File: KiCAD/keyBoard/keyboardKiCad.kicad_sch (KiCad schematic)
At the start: 183 parts, among them SW1 RotaryEncoder_Switch_MP

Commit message: Keyboard routing initially complete
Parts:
- D1, D10, D11, D12, D13, D14, D15, D16, D17, D18, D19, D2, D20, D21, D22, D23, D24, D25, D26, D27, D28, D29, D3, D30, D31, D32, D33, D34, D35, D36, D37, D38, D39, D4, D40, D41, D42, D43, D44, D45, D46, D47, D48, D49, D5, D50, D51, D52, D53, D54, D55, D56, D57, D58, D59, D6, D60, D61, D62, D63, D64, D66, D67, D68, D69, D7, D70, D71, D72, D73, D74, D75, D76, D77, D78, D79, D8, D80, D81, D82, D83, D84, D9: footprint Diode_THT:D_DO-35_SOD27_P10.16mm_Horizontal -> kbProjectLib/lcscImports:DO-35_BD2.0-L4.0-P8.00-D0.5-FD
- S1, S3, S72: footprint PCM_Switch_Keyboard_Kailh:SW_Kailh_Choc_V2_1.50u -> kbProjectLib/keyswitches:SW_Kailh_Choc_V2_1.50u
- S10, S12, S13, S14, S15, S16, S18, S19, S2, S20, S21, S22, S23, S24, S25, S26, S27, S28, S29, S30, S31, S32, S34, S35, S36, S37, S38, S39, S40, S41, S42, S43, S44, S45, S46, S47, S48, S49, S50, S51, S52, S53, S54, S55, S56, S57, S59, S60, S61, S62, S64, S65, S66, S67, S7, S70, S73, S74, S75, S76, S77, S78, S79, S8, S80, S81, S82, S83, S9: footprint PCM_Switch_Keyboard_Kailh:SW_Kailh_Choc_V2_1.00u -> kbProjectLib/keyswitches:SW_Kailh_Choc_V2_1.00u
- S11, S17, S58: footprint PCM_Switch_Keyboard_Kailh:SW_Kailh_Choc_V2_1.25u -> kbProjectLib/keyswitches:SW_Kailh_Choc_V2_1.25u
- S33: footprint PCM_Switch_Keyboard_Kailh:SW_Kailh_Choc_V2_6.25u -> kbProjectLib/keyswitches:SW_Kailh_Choc_V2_6.25u
- S4: footprint PCM_Switch_Keyboard_Kailh:SW_Kailh_Choc_V2_1.75u -> kbProjectLib/keyswitches:SW_Kailh_Choc_V2_1.75u
- S5, S68: footprint PCM_Switch_Keyboard_Kailh:SW_Kailh_Choc_V2_2.25u -> kbProjectLib/keyswitches:SW_Kailh_Choc_V2_2.25u
- S6, S69, S71: footprint PCM_Switch_Keyboard_Kailh:SW_Kailh_Choc_V2_2.00u -> kbProjectLib/keyswitches:SW_Kailh_Choc_V2_2.00u
- S63: footprint PCM_Switch_Keyboard_Kailh:SW_Kailh_Choc_V2_2.75u -> kbProjectLib/keyswitches:SW_Kailh_Choc_V2_2.75u
- SW1: footprint Rotary_Encoder:RotaryEncoder_Alps_EC11E-Switch_Vertical_H20mm -> kbProjectLib/lcscImports:SW-TH_EC11XXXXXXXX
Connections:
- net ROW1: no longer S54.1, S7.1
- net ROW2: now also S54.1, S7.1; no longer S55.1, S8.1
- net ROW3: now also S55.1, S8.1; no longer S56.1, S9.1
- net ROW4: now also S56.1, S9.1; no longer S10.1, S57.1
- net ROW5: now also S10.1, S57.1; no longer S11.1, S58.1
- net ROW6: now also S11.1, S58.1

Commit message: saving before running 3d file fixing script
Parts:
- removed H10, H11, H12, H9: (no value), ScottoKeebs_Stabilizer:Stabilizer_MX_2.00u, symbol ScottoKeebs:Placeholder_Mounting_Hole
- removed H13, H14: (no value), ScottoKeebs_Cutout:Cutout_Stabilizer_3.00u, symbol ScottoKeebs:Placeholder_Mounting_Hole
- removed H15, H16: (no value), ScottoKeebs_Stabilizer:Stabilizer_MX_6.25u, symbol ScottoKeebs:Placeholder_Mounting_Hole
- H1, H2, H3, H4, H5, H6: footprint ScottoKeebs_Stabilizer:Stabilizer_MX_2.00u -> kbProjectLib/keyswitches:Stabilizer_Cherry_MX_2.00u
- H7: footprint ScottoKeebs_Stabilizer:Stabilizer_MX_2.00u -> kbProjectLib/keyswitches:Stabilizer_Cherry_MX_3.00u
- H8: footprint ScottoKeebs_Stabilizer:Stabilizer_MX_2.00u -> kbProjectLib/keyswitches:Stabilizer_Cherry_MX_6.25u
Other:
- moved on the sheet: H6, H7, H8

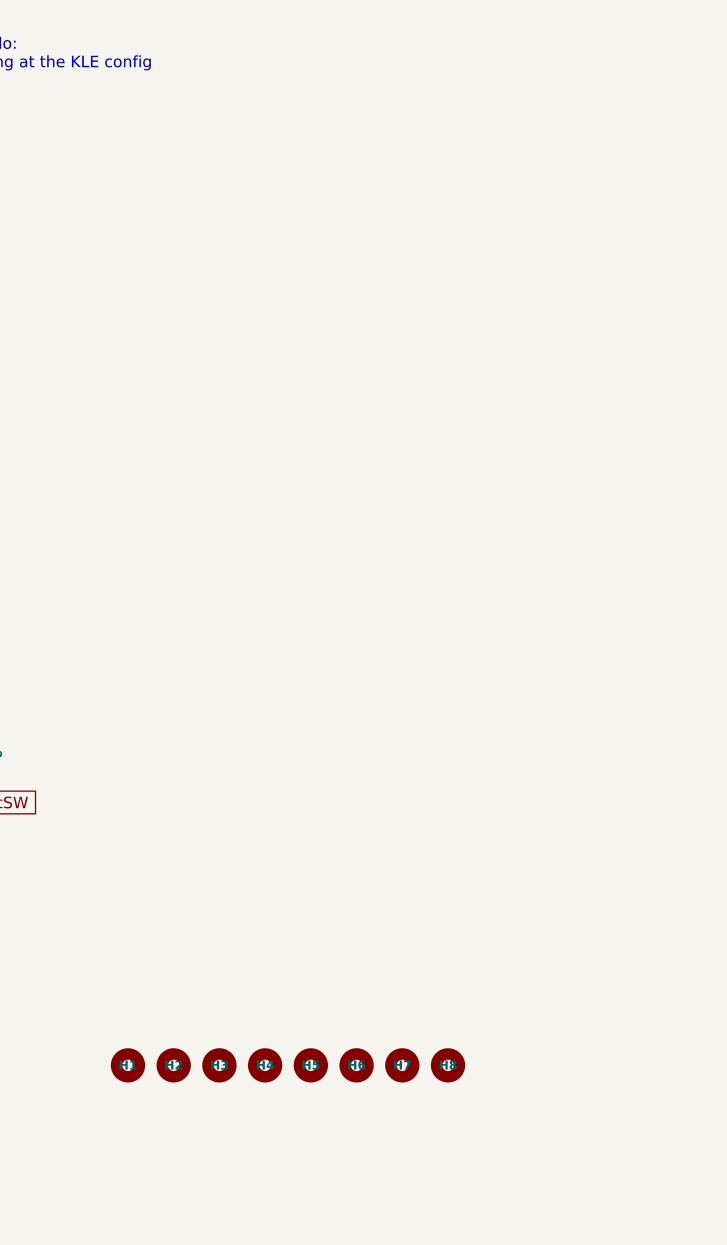
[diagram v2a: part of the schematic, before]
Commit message: MCU board has been mounted on to the keyboard PCB. Need to check if spacing is appropriate irl using calipers. Then do mounting holes using star point grounding due to use with metal chassis. ie seperate net found mounting and ground pours, which only connect at the MCU pin.
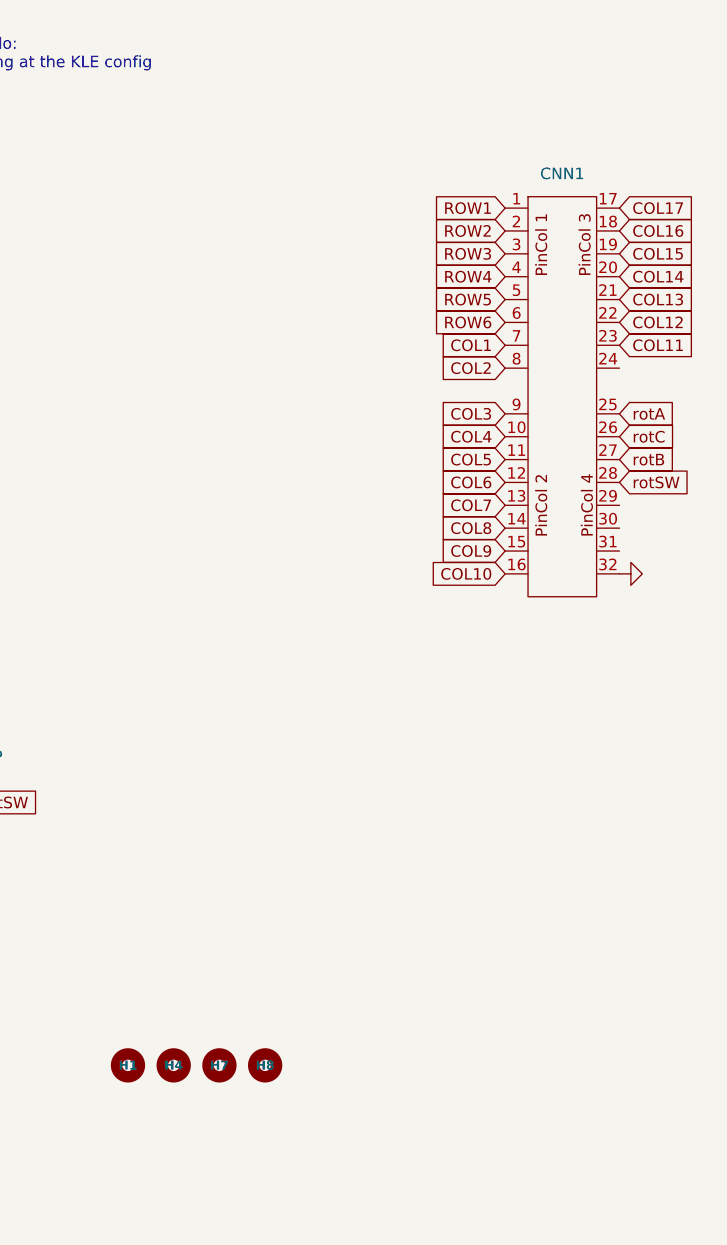
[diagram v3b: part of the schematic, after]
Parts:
- removed H2, H3, H5, H6: (no value), kbProjectLib/keyswitches:Stabilizer_Cherry_MX_2.00u, symbol ScottoKeebs:Placeholder_Mounting_Hole
- added CNN1: (no value), kbProjectLib/mcuConnector:keyboardMCU_Connector, symbol mcuConnector:keyboardMCU_Connector
- D1, D10, D11, D12, D13, D14, D15, D16, D17, D18, D19, D2, D20, D21, D22, D23, D24, D25, D26, D27, D28, D29, D3, D30, D31, D32, D33, D34, D35, D36, D37, D38, D39, D4, D40, D41, D42, D43, D44, D45, D46, D47, D48, D49, D5, D50, D51, D52, D53, D54, D55, D56, D57, D58, D59, D6, D60, D61, D62, D63, D64, D66, D67, D68, D69, D7, D70, D71, D72, D73, D74, D75, D76, D77, D78, D79, D8, D80, D81, D82, D83, D84, D9: LCSC Part (none) -> C258182
- SW1: LCSC Part (none) -> C470742
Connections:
- net COL1: now also CNN1.7
- net COL10: now also CNN1.16
- net COL11: now also CNN1.23
- net COL12: now also CNN1.22
- net COL13: now also CNN1.21
- net COL14: now also CNN1.20
- net COL15: now also CNN1.19
- net COL16: now also CNN1.18
- net COL17: now also CNN1.17
- net COL2: now also CNN1.8
- net COL3: now also CNN1.9
- net COL4: now also CNN1.10
- net COL5: now also CNN1.11
- net COL6: now also CNN1.12
- net COL7: now also CNN1.13
- net COL8: now also CNN1.14
- net COL9: now also CNN1.15
- net GND: now also CNN1.32
- net ROW1: now also CNN1.1
- net ROW2: now also CNN1.2
- net ROW3: now also CNN1.3
- net ROW4: now also CNN1.4
- net ROW5: now also CNN1.5
- net ROW6: now also CNN1.6
- net rotA: now also CNN1.25
- net rotB: now also CNN1.27
- net rotC: now also CNN1.26
- net rotSW: now also CNN1.28
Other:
- moved on the sheet: H4, H7, H8

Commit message: Finished routing, including chassis grounding. One thing, I might need SWD for the MCU. QMK should be able to use USB though. Need to check this.
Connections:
- net GND: now also SW1.E; no longer SW1.S2
- net rotSW: now also SW1.D; no longer SW1.S1
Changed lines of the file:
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@@
 		(pin "MP"
 		)
-		(pin "S2"
+		(pin "D"
 		)
 		(pin "C"
@@
 		(pin "B"
 		)
-		(pin "S1"
+		(pin "E"
 		)
 		(instances
